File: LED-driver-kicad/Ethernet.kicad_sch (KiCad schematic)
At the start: 4 parts, among them U3 ARJM11C7-114-BA-EW2, U7 PD70224ILQ-TR, U8 ENC28J60x-SO, U9 25AA02E64-I/SN

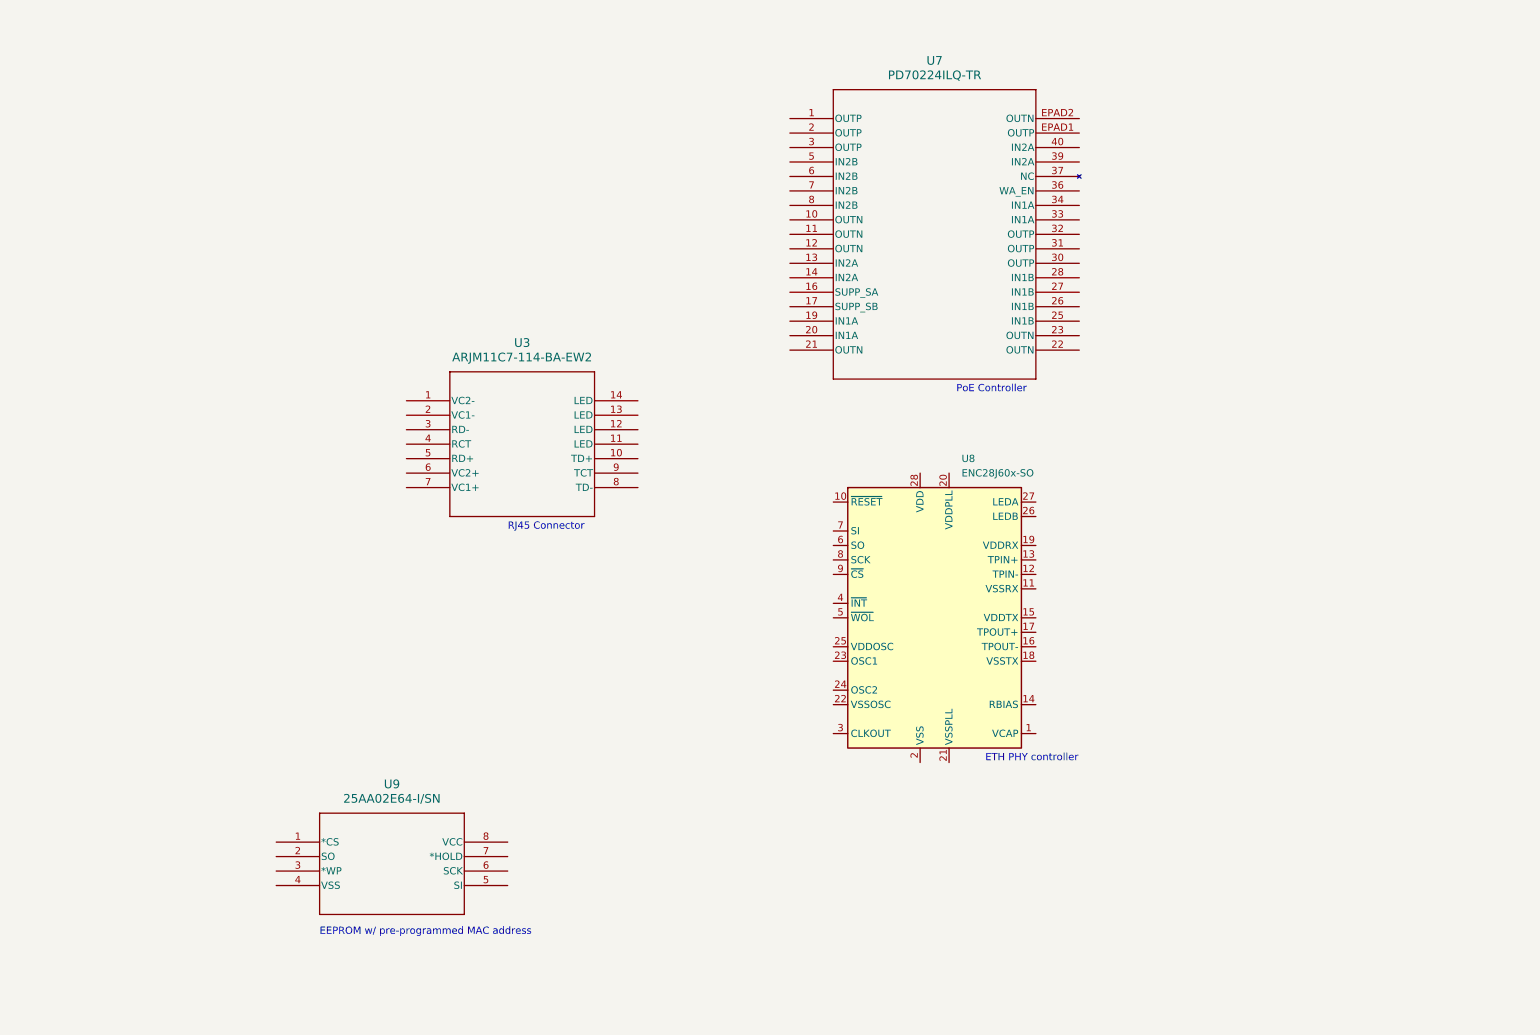
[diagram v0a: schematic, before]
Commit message: chore: update ethernet.kicad_sch
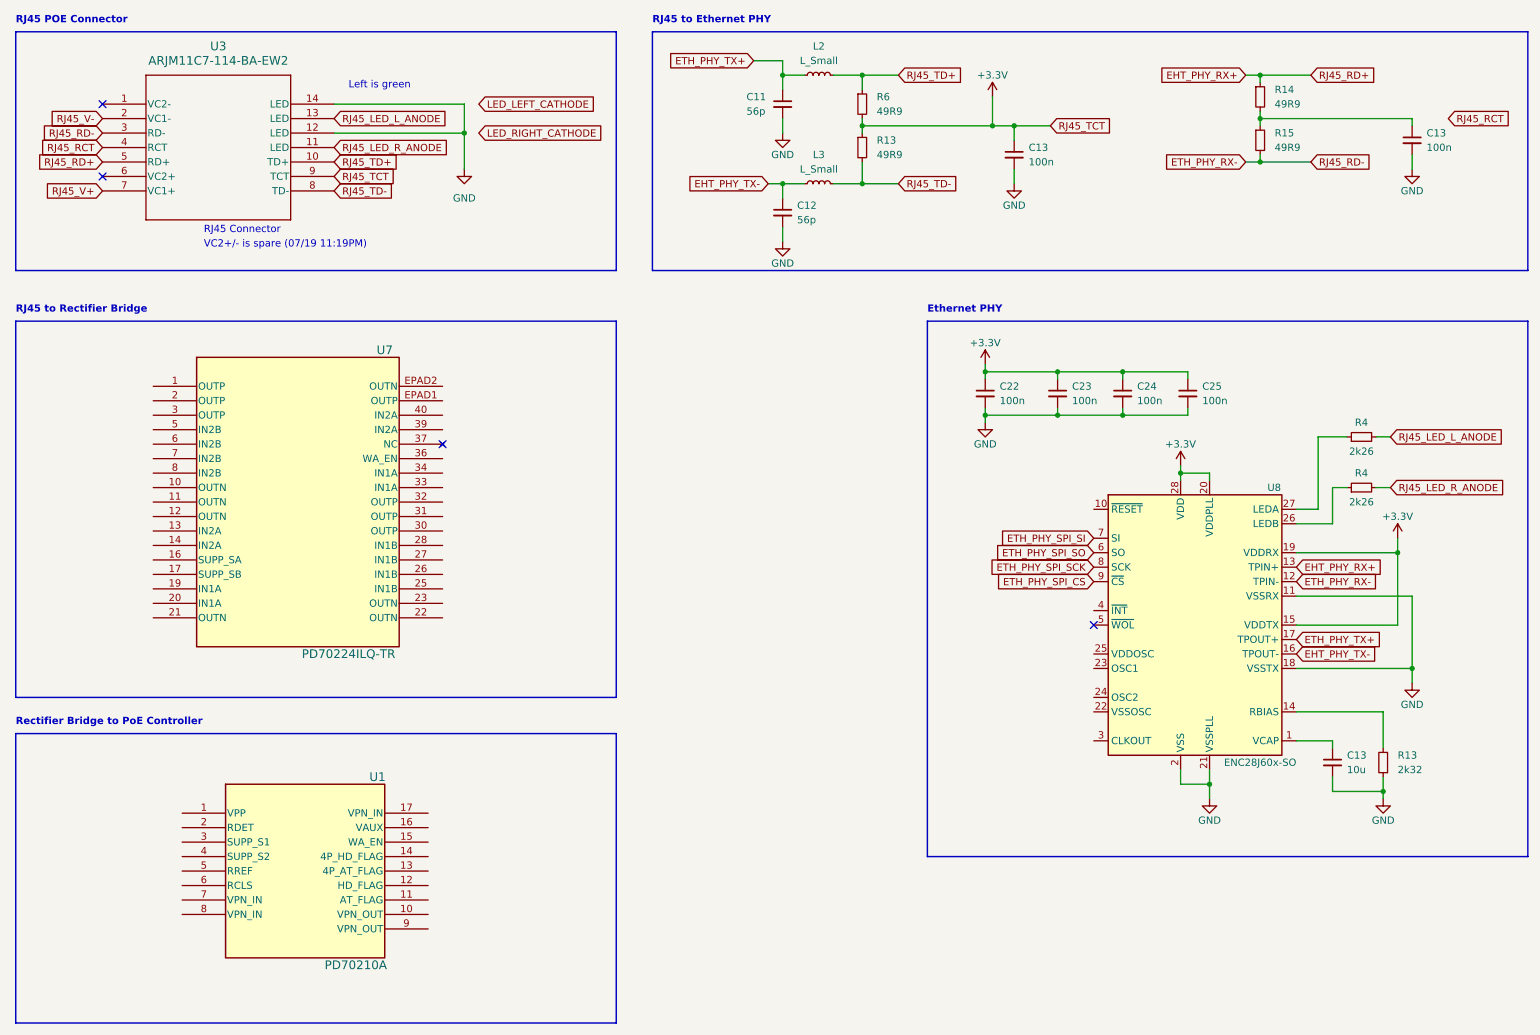
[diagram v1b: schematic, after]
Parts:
- removed U9: 25AA02E64-I/SN, SOIC8_4P9X3P9MC_MCH, symbol 25AA02E64-I/SN:25AA02E64-I_SN
- added C11, C12: 56p, symbol Device:C_Small
- added C13 (x2), C22, C23, C24, C25: 100n, symbol Device:C_Small
- added C13: 10u, symbol Device:C_Small
- added L2, L3: L_Small, symbol Device:L_Small
- added R13: 2k32, symbol Device:R_Small
- added R13, R14, R15, R6: 49R9, symbol Device:R_Small
- added R4 (x2): 2k26, symbol Device:R_Small
- added U1: PD70210A, Mahabeer-Package_DFN_QFN:DFN-16-1EP_4x5mm_P0.5mm_EP2.44x4.34mm-Interface_PoE_Microchip_PD70210A, symbol Interface_PoE_Microchip_PD70210A:PD70210A
- U7: footprint QFN40_6X8_PD70224_MCH -> Package_DFN_QFN:Microsemi_QFN-40-32-2EP_6x8mm_P0.5mm
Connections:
- net at U8.1 (VCAP): now also C13.1
- net GND: now reaches U8.11 (VSSRX)
- net GND: now also U3.12 (LED), U3.14 (LED), U8.18 (VSSTX), U8.2 (VSS), U8.21 (VSSPLL), C11.2, C12.2, C13.2, C13.2, C13.2, C22.2, C23.2, C24.2, C25.2, R13.1
- net ETH_PHY_RX-: now reaches U8.12 (TPIN-)
- net ETH_PHY_RX-: now also U3.3 (RD-), R15.2
- net EHT_PHY_RX+: now reaches U8.13 (TPIN+)
- net EHT_PHY_RX+: now also U3.5 (RD+), R14.1
- net at U8.14 (RBIAS): now also R13.2
- net +3.3V: now reaches U8.15 (VDDTX)
- net +3.3V: now also U3.9 (TCT), U8.19 (VDDRX), U8.20 (VDDPLL), U8.28 (VDD), C13.1, C22.1, C23.1, C24.1, C25.1, R13.1, R6.2
- net EHT_PHY_TX-: now reaches U8.16 (TPOUT-)
- net EHT_PHY_TX-: now also C12.1, L3.1
- net ETH_PHY_TX+: now reaches U8.17 (TPOUT+)
- net ETH_PHY_TX+: now also C11.1, L2.1
- net at U8.26 (LEDB): now also R4.1
- net at U8.27 (LEDA): now also R4.1
- net ETH_PHY_SPI_SO: now reaches U8.6 (SO)
- net ETH_PHY_SPI_SI: now reaches U8.7 (SI)
- net ETH_PHY_SPI_SCK: now reaches U8.8 (SCK)
- net ETH_PHY_SPI_CS: now reaches U8.9 (~{CS})
- net RJ45_TD+: now reaches U3.10 (TD+)
- net RJ45_TD+: now also L2.2, R6.1
- net RJ45_LED_R_ANODE: now reaches U3.11 (LED)
- net RJ45_LED_R_ANODE: now also R4.2
- net RJ45_LED_L_ANODE: now reaches U3.13 (LED)
- net RJ45_LED_L_ANODE: now also R4.2
- net RJ45_V-: now reaches U3.2 (VC1-)
- net RJ45_RCT: now reaches U3.4 (RCT)
- net RJ45_V+: now reaches U3.7 (VC1+)
- net RJ45_TD-: now reaches U3.8 (TD-)
- net RJ45_TD-: now also L3.2, R13.2
- new net: C13.1, R14.2, R15.1
- no-connect marks 0 -> 4
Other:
- note added: "Ethernet PHY"
- note added: "Left is green"
- note added: "RJ45 POE Connector"
- note added: "RJ45 to Ethernet PHY"
- note added: "RJ45 to Rectifier Bridge"
- note added: "Rectifier Bridge to PoE Controller"
- note added: "VC2+/- is spare (07/19 11:19PM)"
- note removed: "EEPROM w/ pre-programmed MAC address"
- note removed: "ETH PHY controller"
- note removed: "PoE Controller"
- moved on the sheet: U3, U8

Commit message: update ENC28J60x-SO circuit
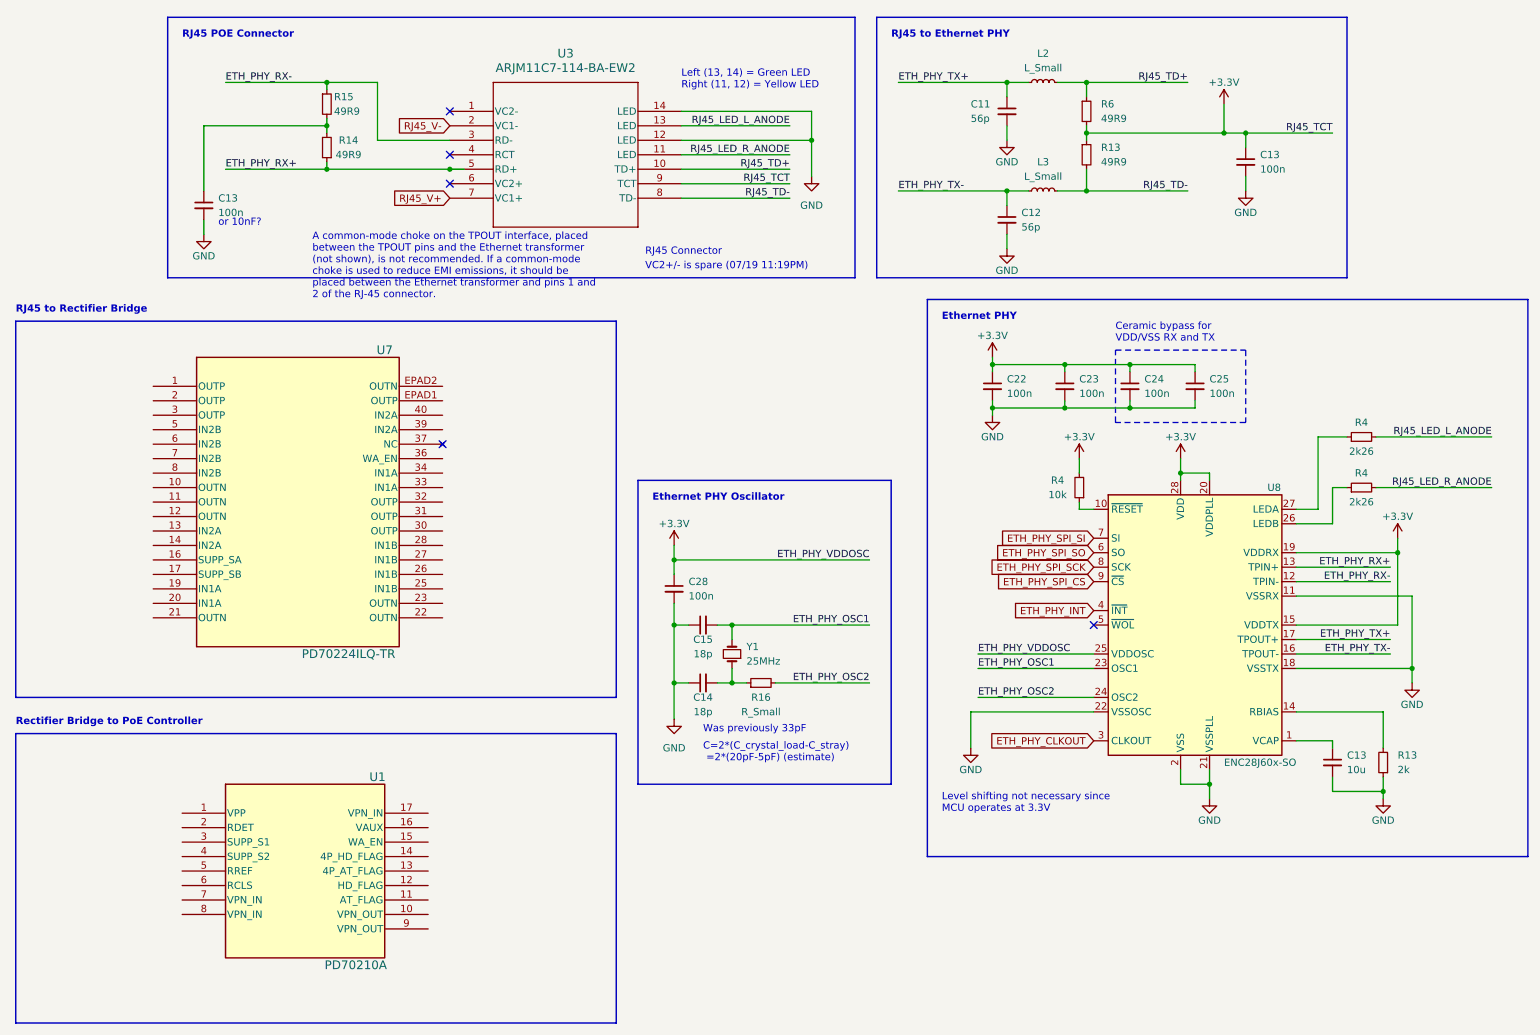
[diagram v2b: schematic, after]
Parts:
- added C14, C15: 18p, symbol Device:C_Small
- added C28: 100n, symbol Device:C_Small
- added R16: R_Small, symbol Device:R_Small
- added R4: 10k, symbol Device:R_Small
- added Y1: 25MHz, symbol Device:Crystal_Small
- R13: value 2k32 -> 2k
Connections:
- net +3.3V: now also U8.25 (VDDOSC), C28.1, R4.2
- net ETH_PHY_RX-: now also R15.1; no longer R15.2
- net GND: now also U8.22 (VSSOSC), C14.1, C15.1, C28.2
- net at U8.10 (~{RESET}): now also R4.1
- net ETH_PHY_OSC1: now reaches U8.23 (OSC1)
- net ETH_PHY_OSC1: now also C15.2, Y1.2
- net ETH_PHY_OSC2: now reaches U8.24 (OSC2)
- net ETH_PHY_OSC2: now also R16.2
- net ETH_PHY_CLKOUT: now reaches U8.3 (CLKOUT)
- net ETH_PHY_INT: now reaches U8.4 (~{INT})
- net at C13.1, R14.2: now also R15.2; no longer R15.1
- net EHT_PHY_RX+ renamed ETH_PHY_RX+
- net EHT_PHY_TX- renamed ETH_PHY_TX-
- net RJ45_RCT: no longer names the net of U3.4 (RCT)
- new net: C14.2, R16.1, Y1.1
- no-connect marks 4 -> 5
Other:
- note added: "A common-mode choke on the TPOUT interface, placed between the TPOUT pins and the Ethernet transformer (not shown), is not recommended. If a common-mode choke is used to reduce EMI emissions, it should be placed between the Ethernet transformer and pins 1 and 2 of the RJ-45 connector."
- note added: "C=2*(C_crystal_load-C_stray) =2*(20pF-5pF) (estimate)"
- note added: "Ceramic bypass for VDD/VSS RX and TX"
- note added: "Ethernet PHY Oscillator"
- note added: "Left (13, 14) = Green LED Right (11, 12) = Yellow LED"
- note added: "Level shifting not necessary since MCU operates at 3.3V"
- note added: "Was previously 33pF"
- note added: "or 10nF?"
- note removed: "Left is green"
- moved on the sheet: C11, C12, C13, C22, C23, C24, C25, L2, L3, R13, R14, R15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

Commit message: update schematic for RJ45 connector and Ethernet controller
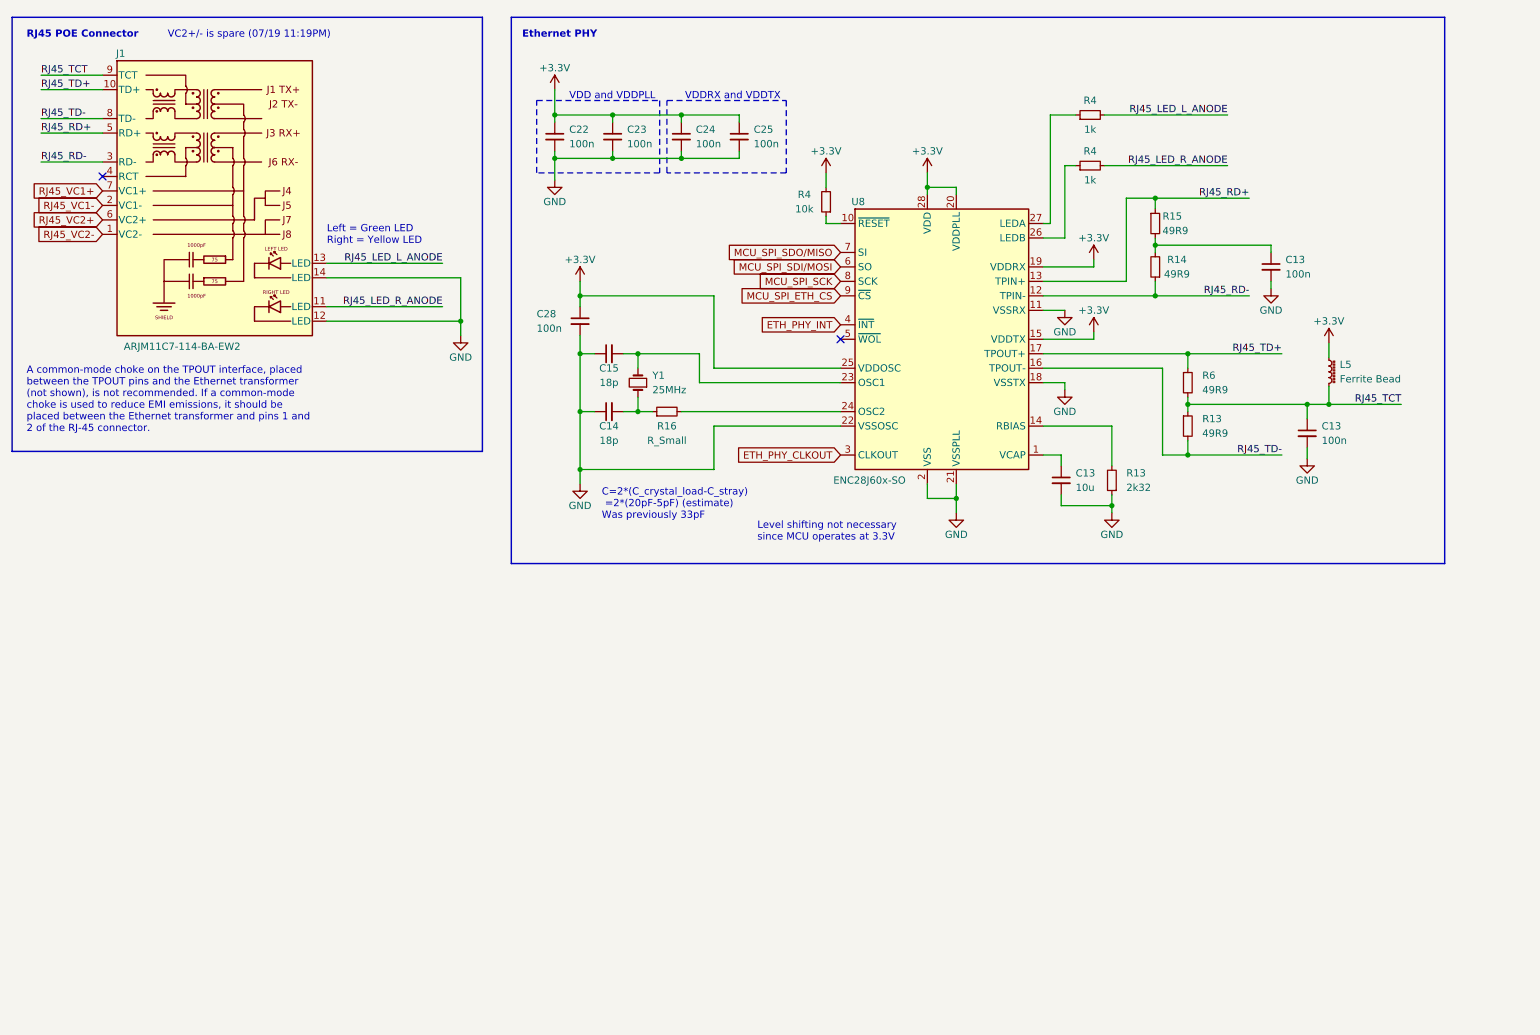
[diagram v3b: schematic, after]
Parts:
- removed C11, C12: 56p, symbol Device:C_Small
- removed L2, L3: L_Small, symbol Device:L_Small
- removed U1: PD70210A, Mahabeer-Package_DFN_QFN:DFN-16-1EP_4x5mm_P0.5mm_EP2.44x4.34mm-Interface_PoE_Microchip_PD70210A, symbol Interface_PoE_Microchip_PD70210A:PD70210A
- removed U3: ARJM11C7-114-BA-EW2, ARJM11C7-114-BA-EW2_ABR, symbol Abracon_ARJM11C7-114-BA-EW2:ARJM11C7-114-BA-EW2
- removed U7: PD70224ILQ-TR, Package_DFN_QFN:Microsemi_QFN-40-32-2EP_6x8mm_P0.5mm, symbol Microchip_PD70224ILQ-TR:PD70224ILQ-TR
- added J1: ARJM11C7-114-BA-EW2, Connector_RJ:Connector_RJ45_Abracon_ARJM11C7-114-BA-EW2, symbol Connector_RJ45_Abracon_ARJM11C7-114-BA-EW2:ARJM11C7-114-BA-EW2_1
- added L5: Ferrite Bead, symbol Device:L_Ferrite_Small
- R13: value 2k -> 2k32
- R4: value 2k26 -> 1k
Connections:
- net ETH_PHY_TX+ is gone; now on net RJ45_TD+: U8.17 (TPOUT+)
- net ETH_PHY_TX- is gone; now on net RJ45_TD-: U8.16 (TPOUT-)
- net +3.3V: now also L5.1; no longer C13.1, R13.1, R6.2
- net GND: now also J1.12 (LED), J1.14 (LED)
- net RJ45_LED_L_ANODE: now also J1.13 (LED)
- net RJ45_LED_R_ANODE: now also J1.11 (LED)
- net RJ45_TD+: now also J1.10 (TD+)
- net RJ45_TD-: now also J1.8 (TD-)
- net ETH_PHY_OSC1: no longer names the net of C15.2, U8.23 (OSC1), Y1.2
- net ETH_PHY_OSC2: no longer names the net of R16.2, U8.24 (OSC2)
- net ETH_PHY_RX+ renamed RJ45_RD+
- net RJ45_RD+: now also R15.1, J1.5 (RD+); no longer R14.1
- net ETH_PHY_RX- renamed RJ45_RD-
- net RJ45_RD-: now also R14.1, J1.3 (RD-); no longer R15.1
- net ETH_PHY_SPI_CS renamed MCU_SPI_ETH_CS
- net ETH_PHY_SPI_SCK renamed MCU_SPI_SCK
- net ETH_PHY_SPI_SI renamed MCU_SPI_SDO/MISO
- net ETH_PHY_SPI_SO renamed MCU_SPI_SDI/MOSI
- new net RJ45_TCT: C13.1, J1.9 (TCT), L5.2, R13.1, R6.2
- new net RJ45_VC1+: J1.7 (VC1+)
- new net RJ45_VC1-: J1.2 (VC1-)
- new net RJ45_VC2+: J1.6 (VC2+)
- new net RJ45_VC2-: J1.1 (VC2-)
- no-connect marks 5 -> 2
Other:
- note added: "C=2*(C_crystal_load-C_stray) =2*(20pF-5pF) (estimate) Was previously 33pF"
- note added: "Left = Green LED Right = Yellow LED"
- note added: "VDD and VDDPLL"
- note added: "VDDRX and VDDTX"
- note removed: "C=2*(C_crystal_load-C_stray) =2*(20pF-5pF) (estimate)"
- note removed: "Ceramic bypass for VDD/VSS RX and TX"
- note removed: "Ethernet PHY Oscillator"
- note removed: "Left (13, 14) = Green LED Right (11, 12) = Yellow LED"
- note removed: "RJ45 Connector"
- note removed: "RJ45 to Ethernet PHY"
- note removed: "RJ45 to Rectifier Bridge"
- note removed: "Rectifier Bridge to PoE Controller"
- note removed: "Was previously 33pF"
- note removed: "or 10nF?"
- moved on the sheet: C13, C14, C15, C22, C23, C24, C25, C28, R13, R16, R4, R6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
